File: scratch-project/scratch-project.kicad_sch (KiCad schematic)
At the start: 18 parts, among them J1 Conn_01x10_Pin, J2 Conn_01x10_Pin, J3 Conn_02x10_Top_Bottom, J4 Conn_02x10_Top_Bottom, J5 Conn_02x10_Top_Bottom, J6 Conn_01x10_Pin, J7 Conn_02x05_Top_Bottom, J8 Conn_02x10_Top_Bottom, J9 Conn_02x10_Top_Bottom

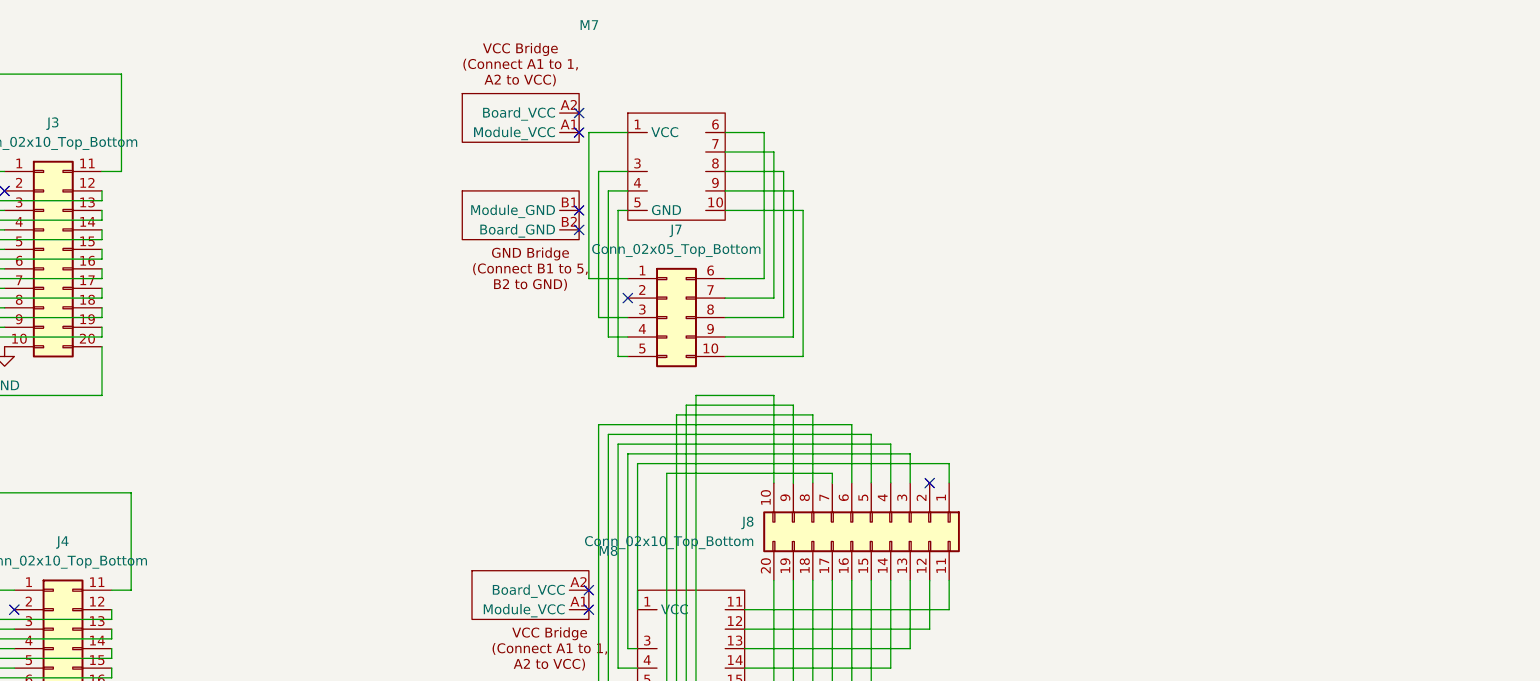
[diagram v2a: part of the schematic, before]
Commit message: finish adding dummy modules to scratch board
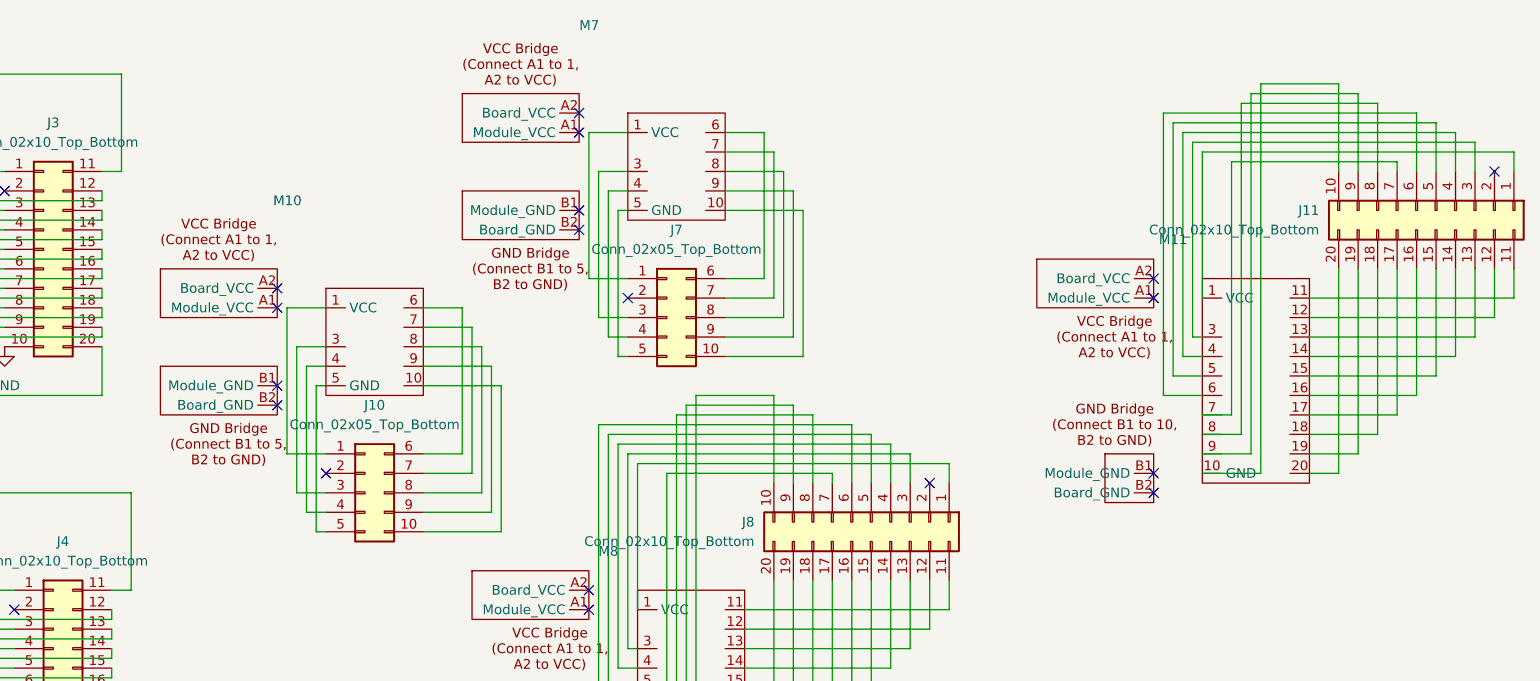
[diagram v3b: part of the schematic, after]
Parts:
- added J10: Conn_02x05_Top_Bottom, Connector_PinHeader_1.27mm:PinHeader_2x05_P1.27mm_Vertical, symbol Connector_Generic:Conn_02x05_Top_Bottom
- added J11: Conn_02x10_Top_Bottom, Connector_PinHeader_1.27mm:PinHeader_2x10_P1.27mm_Vertical, symbol Connector_Generic:Conn_02x10_Top_Bottom
- added M10: ~, MegaCastle:MegaCastle2x5-Module, symbol MegaCastle:MegaCastle2x5
- added M11: ~, MegaCastle:MegaCastle2x10Wide-Module, symbol MegaCastle:MegaCastle2x10
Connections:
- new net: J11.1 (Pin_1), M11.1 (VCC)
- new net: J11.10 (Pin_10), M11.10 (GND)
- new net: J11.11 (Pin_11), M11.11
- new net: J11.12 (Pin_12), M11.12
- new net: J11.13 (Pin_13), M11.13
- new net: J11.14 (Pin_14), M11.14
- new net: J11.15 (Pin_15), M11.15
- new net: J11.16 (Pin_16), M11.16
- new net: J11.17 (Pin_17), M11.17
- new net: J11.18 (Pin_18), M11.18
- new net: J11.19 (Pin_19), M11.19
- new net: J11.20 (Pin_20), M11.20
- new net: J11.3 (Pin_3), M11.3
- new net: J11.4 (Pin_4), M11.4
- new net: J11.5 (Pin_5), M11.5
- new net: J11.6 (Pin_6), M11.6
- new net: J11.7 (Pin_7), M11.7
- new net: J11.8 (Pin_8), M11.8
- new net: J11.9 (Pin_9), M11.9
- new net: J10.1 (Pin_1), M10.1 (VCC)
- new net: J10.10 (Pin_10), M10.10
- new net: J10.3 (Pin_3), M10.3
- new net: J10.4 (Pin_4), M10.4
- new net: J10.5 (Pin_5), M10.5 (GND)
- new net: J10.6 (Pin_6), M10.6
- new net: J10.7 (Pin_7), M10.7
- new net: J10.8 (Pin_8), M10.8
- new net: J10.9 (Pin_9), M10.9
- no-connect marks 19 -> 29

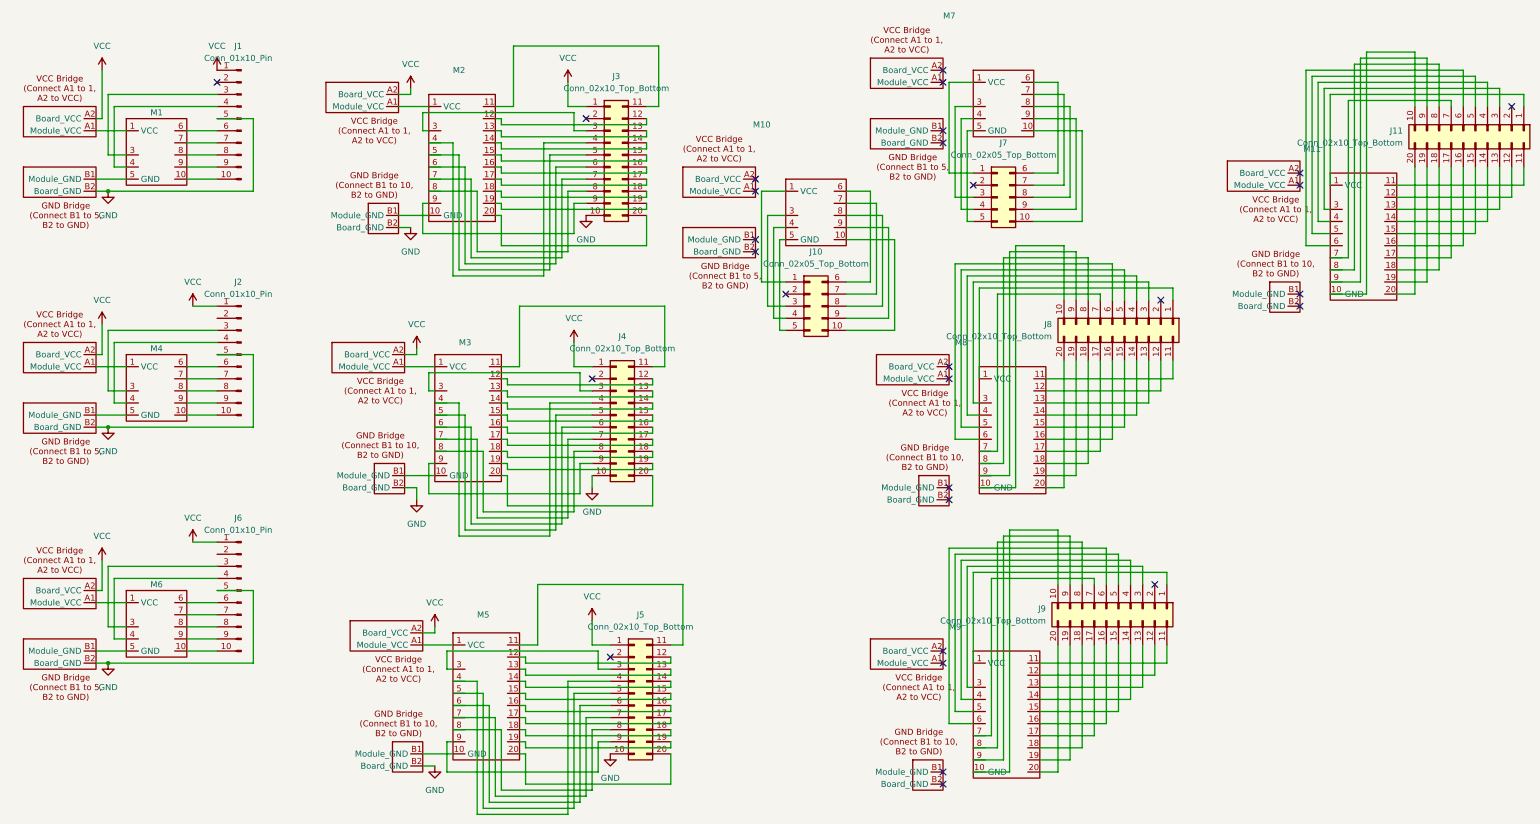
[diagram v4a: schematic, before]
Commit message: update scratch project to have current module footprints
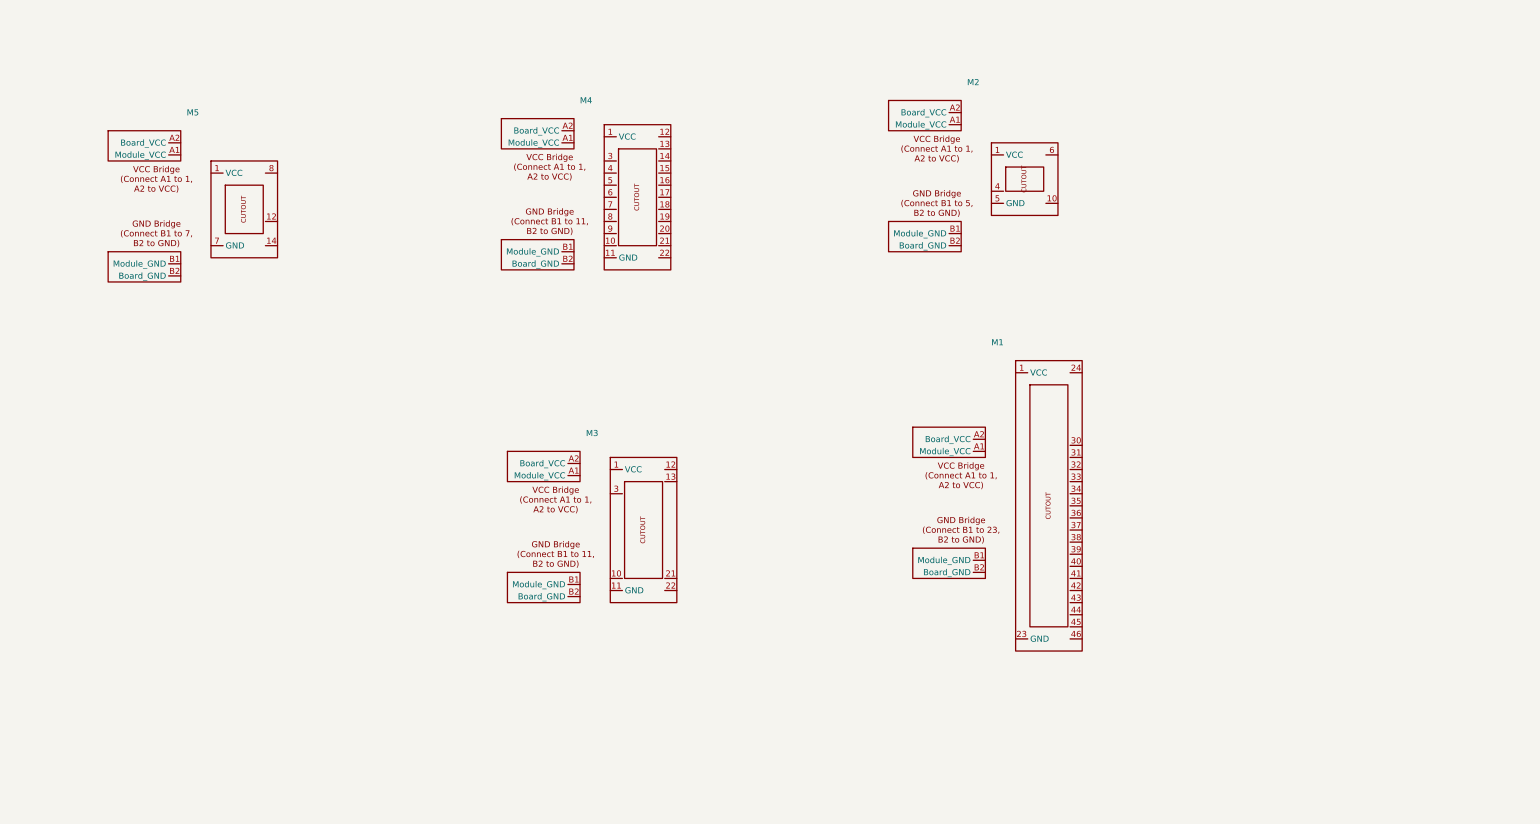
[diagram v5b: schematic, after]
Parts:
- removed J1, J2, J6: Conn_01x10_Pin, Connector_PinHeader_2.54mm:PinHeader_1x10_P2.54mm_Vertical, symbol Connector:Conn_01x10_Pin
- removed J10, J7: Conn_02x05_Top_Bottom, Connector_PinHeader_1.27mm:PinHeader_2x05_P1.27mm_Vertical, symbol Connector_Generic:Conn_02x05_Top_Bottom
- removed J11, J8, J9: Conn_02x10_Top_Bottom, Connector_PinHeader_1.27mm:PinHeader_2x10_P1.27mm_Vertical, symbol Connector_Generic:Conn_02x10_Top_Bottom
- removed J3, J4, J5: Conn_02x10_Top_Bottom, Connector_PinHeader_2.54mm:PinHeader_2x10_P2.54mm_Vertical, symbol Connector_Generic:Conn_02x10_Top_Bottom
- removed M1, M4, M6: ~, MegaCastle:MegaCastle2x5, symbol MegaCastle:MegaCastle2x5
- removed M10, M7: ~, MegaCastle:MegaCastle2x5-Module, symbol MegaCastle:MegaCastle2x5
- removed M11, M9: ~, MegaCastle:MegaCastle2x10Wide-Module, symbol MegaCastle:MegaCastle2x10
- removed M2, M5: ~, MegaCastle:MegaCastle2x10Wide, symbol MegaCastle:MegaCastle2x10
- removed M3: ~, MegaCastle:MegaCastle2x10, symbol MegaCastle:MegaCastle2x10
- removed M8: ~, MegaCastle:MegaCastle2x10-Module, symbol MegaCastle:MegaCastle2x10
- added M1: ~, MegaCastle:MegaCastle2x23-I30.0x53.6-M80000307FFFC, symbol MegaCastle:MegaCastle2x23-I30.0x53.6-M80000307FFFC
- added M2: ~, MegaCastle:MegaCastle2x5-I6.4x7.9-M9C4, symbol MegaCastle:MegaCastle2x5-I6.4x7.9-M9C4
- added M3: ~, MegaCastle:MegaCastle2x11-I15.7x23.1-MA0780C, symbol MegaCastle:MegaCastle2x11-I15.7x23.1-MA0780C
- added M4: ~, MegaCastle:MegaCastle2x11-I17.7x23.1-MBFFFFC, symbol MegaCastle:MegaCastle2x11-I17.7x23.1-MBFFFFC
- added M5: ~, MegaCastle:MegaCastle2x7-I12.7x13.0-M8314, symbol MegaCastle:MegaCastle2x7-I12.7x13.0-M8314
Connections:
- no-connect marks 29 -> 0
